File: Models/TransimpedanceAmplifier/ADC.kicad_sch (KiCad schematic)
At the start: 9 parts, among them U3 ADS8699IPW

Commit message: Save progress
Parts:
- U3: footprint PW16_TEX -> (none)
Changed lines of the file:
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@@
 			)
 		)
-		(property "Footprint" "PW16_TEX"
+		(property "Footprint" ""
 			(at 68.58 50.8 0)
 			(effects

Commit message: Save progress
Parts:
- U3: value ADS8699IPW -> ADS8699
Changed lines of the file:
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@@
 			)
 		)
-		(property "Value" "ADS8699IPW"
+		(property "Value" "ADS8699"
 			(at 104.14 43.18 0)
 			(effects

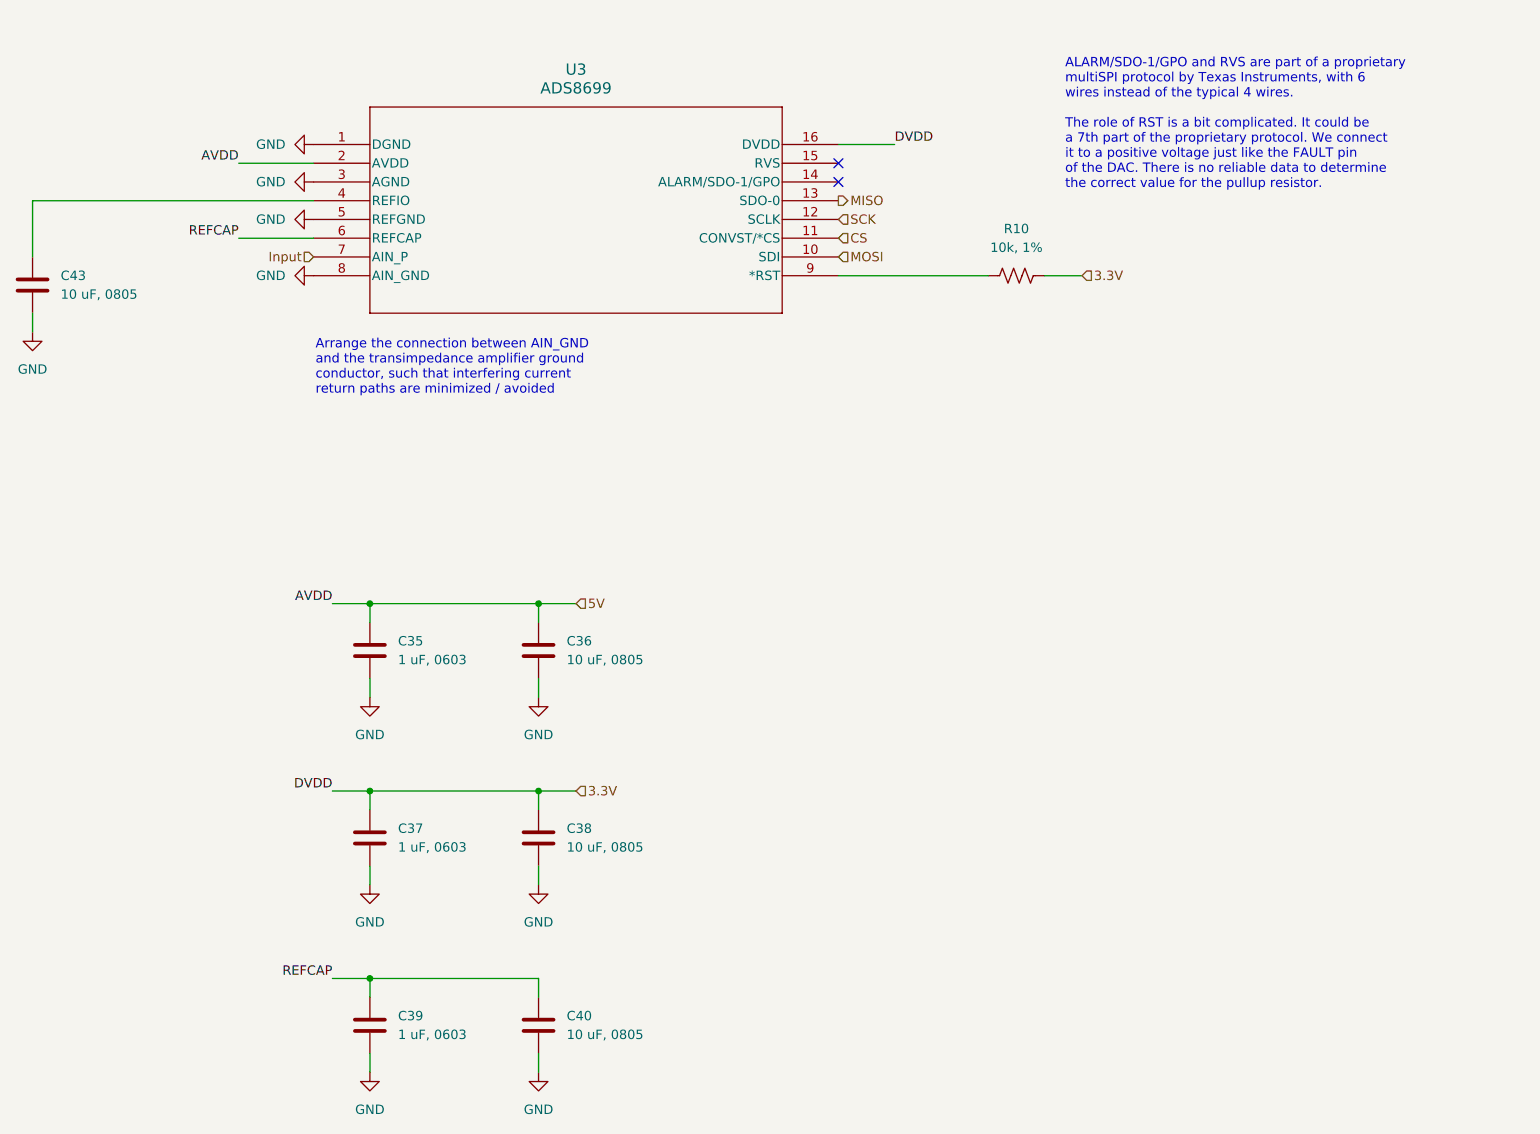
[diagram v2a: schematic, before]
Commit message: Overhauled all of the annotations
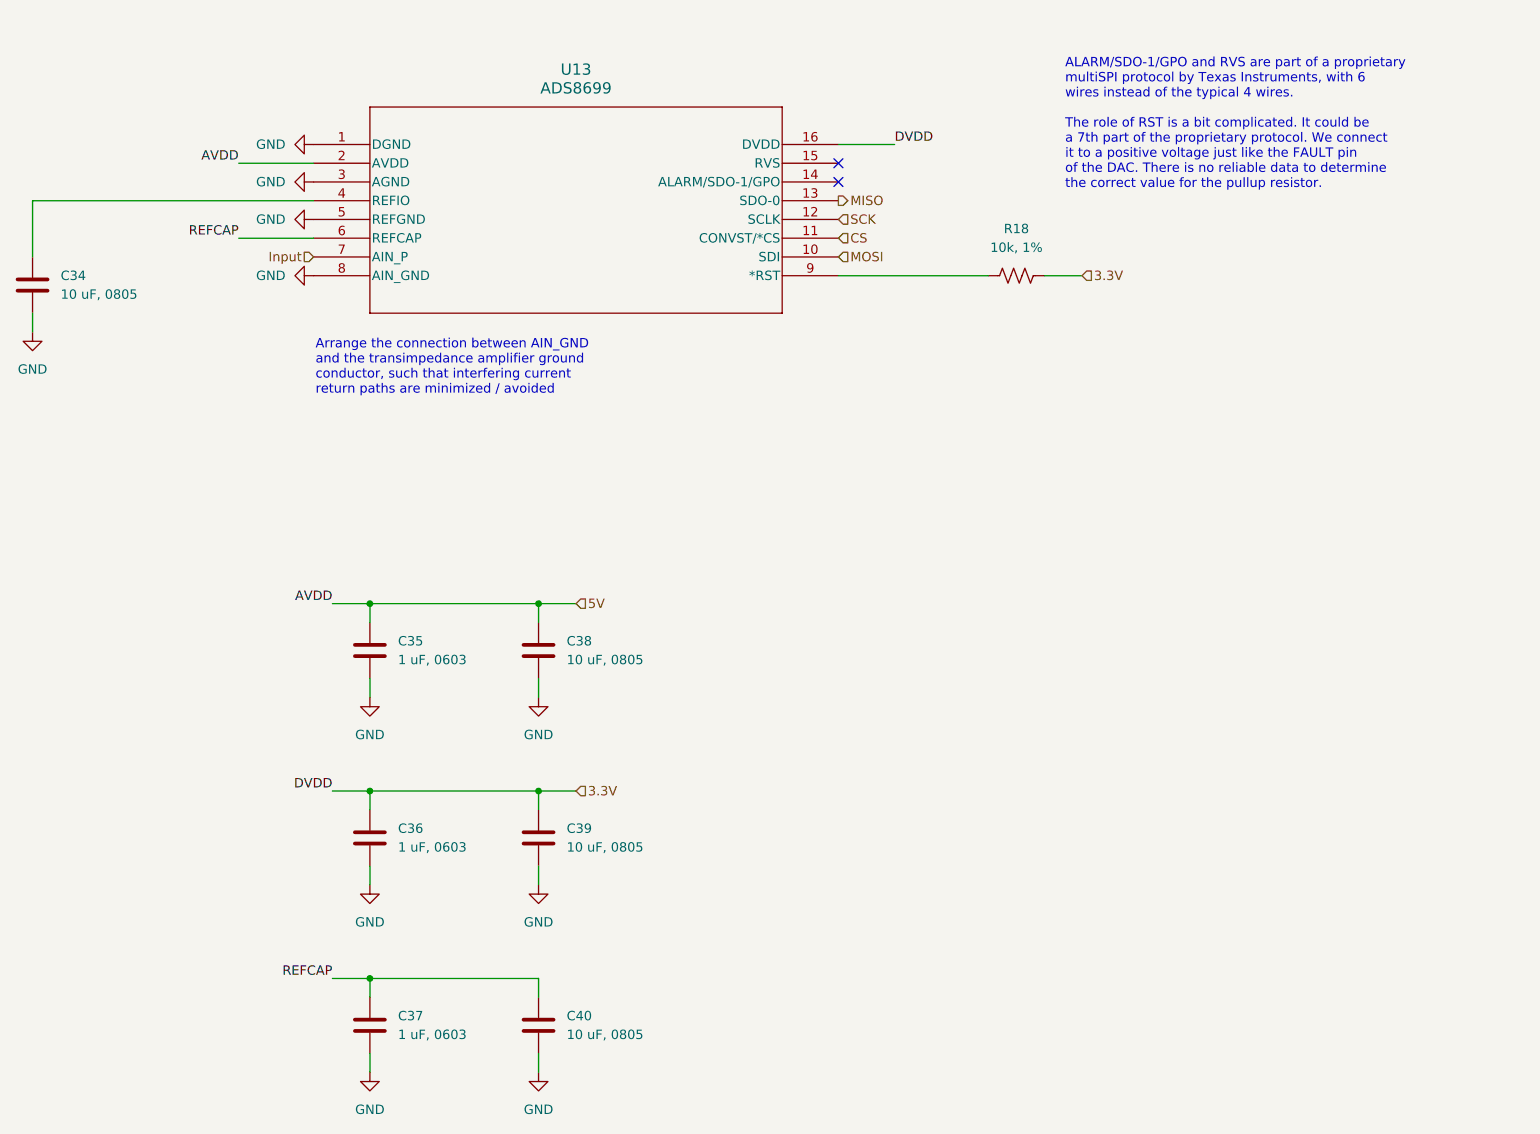
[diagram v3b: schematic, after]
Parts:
- renumbered C43 to C34, C37 to C36, C39 to C37, C36 to C38, C38 to C39, R10 to R18, U3 to U13
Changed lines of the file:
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@@
 		(dnp no)
 		(fields_autoplaced yes)
-		(property "Reference" "#PWR054"
+		(property "Reference" "#PWR056"
 			(at 99.06 182.88 0)
 			(effects
@@
 			(project "TransimpedanceAmplifier"
 				(path "/ec9f2ae3-e40d-40eb-9760-2b611ee8efd1/7e303428-a18c-4ad4-b002-5ab9c6631588/4e36751c-3edc-4fd3-bdbc-fcba4fce50b6"
-					(reference "#PWR054")
+					(reference "#PWR056")
 					(unit 1)
 				)
@@
 		(dnp no)
 		(fields_autoplaced yes)
-		(property "Reference" "#PWR051"
+		(property "Reference" "#PWR052"
 			(at 76.2 157.48 0)
 			(effects
@@
 			(project "TransimpedanceAmplifier"
 				(path "/ec9f2ae3-e40d-40eb-9760-2b611ee8efd1/7e303428-a18c-4ad4-b002-5ab9c6631588/4e36751c-3edc-4fd3-bdbc-fcba4fce50b6"
-					(reference "#PWR051")
+					(reference "#PWR052")
 					(unit 1)
 				)
@@
 		(dnp no)
 		(fields_autoplaced yes)
-		(property "Reference" "U3"
+		(property "Reference" "U13"
 			(at 104.14 40.64 0)
 			(effects
@@
 			(project ""
 				(path "/ec9f2ae3-e40d-40eb-9760-2b611ee8efd1/7e303428-a18c-4ad4-b002-5ab9c6631588/4e36751c-3edc-4fd3-bdbc-fcba4fce50b6"
-					(reference "U3")
+					(reference "U13")
 					(unit 1)
 				)
@@
 		(dnp no)
 		(fields_autoplaced yes)
-		(property "Reference" "#PWR057"
+		(property "Reference" "#PWR046"
 			(at 30.48 82.55 0)
 			(effects
@@
 			(project ""
 				(path "/ec9f2ae3-e40d-40eb-9760-2b611ee8efd1/7e303428-a18c-4ad4-b002-5ab9c6631588/4e36751c-3edc-4fd3-bdbc-fcba4fce50b6"
-					(reference "#PWR057")
+					(reference "#PWR046")
 					(unit 1)
 				)
@@
 		(dnp no)
 		(fields_autoplaced yes)
-		(property "Reference" "#PWR052"
+		(property "Reference" "#PWR055"
 			(at 99.06 157.48 0)
 			(effects
@@
 			(project "TransimpedanceAmplifier"
 				(path "/ec9f2ae3-e40d-40eb-9760-2b611ee8efd1/7e303428-a18c-4ad4-b002-5ab9c6631588/4e36751c-3edc-4fd3-bdbc-fcba4fce50b6"
-					(reference "#PWR052")
+					(reference "#PWR055")
 					(unit 1)
 				)
@@
 		(dnp no)
 		(fields_autoplaced yes)
-		(property "Reference" "C39"
+		(property "Reference" "C37"
 			(at 80.01 168.9099 0)
 			(effects
@@
 			(project "TransimpedanceAmplifier"
 				(path "/ec9f2ae3-e40d-40eb-9760-2b611ee8efd1/7e303428-a18c-4ad4-b002-5ab9c6631588/4e36751c-3edc-4fd3-bdbc-fcba4fce50b6"
-					(reference "C39")
+					(reference "C37")
 					(unit 1)
 				)
@@
 		(dnp no)
 		(fields_autoplaced yes)
-		(property "Reference" "C38"
+		(property "Reference" "C39"
 			(at 102.87 143.5099 0)
 			(effects
@@
 			(project "TransimpedanceAmplifier"
 				(path "/ec9f2ae3-e40d-40eb-9760-2b611ee8efd1/7e303428-a18c-4ad4-b002-5ab9c6631588/4e36751c-3edc-4fd3-bdbc-fcba4fce50b6"
-					(reference "C38")
+					(reference "C39")
 					(unit 1)
 				)
@@
 		(dnp no)
 		(fields_autoplaced yes)
-		(property "Reference" "C37"
+		(property "Reference" "C36"
 			(at 80.01 143.5099 0)
 			(effects
@@
 			(project "TransimpedanceAmplifier"
 				(path "/ec9f2ae3-e40d-40eb-9760-2b611ee8efd1/7e303428-a18c-4ad4-b002-5ab9c6631588/4e36751c-3edc-4fd3-bdbc-fcba4fce50b6"
-					(reference "C37")
+					(reference "C36")
 					(unit 1)
 				)
@@
 		(dnp no)
 		(fields_autoplaced yes)
-		(property "Reference" "#PWR017"
+		(property "Reference" "#PWR050"
 			(at 62.23 68.58 0)
 			(effects
@@
 			(project ""
 				(path "/ec9f2ae3-e40d-40eb-9760-2b611ee8efd1/7e303428-a18c-4ad4-b002-5ab9c6631588/4e36751c-3edc-4fd3-bdbc-fcba4fce50b6"
-					(reference "#PWR017")
+					(reference "#PWR050")
 					(unit 1)
 				)
@@
 		(dnp no)
 		(fields_autoplaced yes)
-		(property "Reference" "C36"
+		(property "Reference" "C38"
 			(at 102.87 118.1099 0)
 			(effects
@@
 			(project "TransimpedanceAmplifier"
 				(path "/ec9f2ae3-e40d-40eb-9760-2b611ee8efd1/7e303428-a18c-4ad4-b002-5ab9c6631588/4e36751c-3edc-4fd3-bdbc-fcba4fce50b6"
-					(reference "C36")
+					(reference "C38")
 					(unit 1)
 				)
@@
 		(dnp no)
 		(fields_autoplaced yes)
-		(property "Reference" "#PWR050"
+		(property "Reference" "#PWR054"
 			(at 99.06 132.08 0)
 			(effects
@@
 			(project "TransimpedanceAmplifier"
 				(path "/ec9f2ae3-e40d-40eb-9760-2b611ee8efd1/7e303428-a18c-4ad4-b002-5ab9c6631588/4e36751c-3edc-4fd3-bdbc-fcba4fce50b6"
-					(reference "#PWR050")
+					(reference "#PWR054")
 					(unit 1)
 				)
@@
 		(dnp no)
 		(fields_autoplaced yes)
-		(property "Reference" "#PWR049"
+		(property "Reference" "#PWR051"
 			(at 76.2 132.08 0)
 			(effects
@@
 			(project ""
 				(path "/ec9f2ae3-e40d-40eb-9760-2b611ee8efd1/7e303428-a18c-4ad4-b002-5ab9c6631588/4e36751c-3edc-4fd3-bdbc-fcba4fce50b6"
-					(reference "#PWR049")
+					(reference "#PWR051")
 					(unit 1)
 				)
@@
 		(dnp no)
 		(fields_autoplaced yes)
-		(property "Reference" "C43"
+		(property "Reference" "C34"
 			(at 34.29 68.5799 0)
 			(effects
@@
 			(project ""
 				(path "/ec9f2ae3-e40d-40eb-9760-2b611ee8efd1/7e303428-a18c-4ad4-b002-5ab9c6631588/4e36751c-3edc-4fd3-bdbc-fcba4fce50b6"
-					(reference "C43")
+					(reference "C34")
 					(unit 1)
 				)
@@
 		(dnp no)
 		(fields_autoplaced yes)
-		(property "Reference" "#PWR018"
+		(property "Reference" "#PWR049"
 			(at 62.23 60.96 0)
 			(effects
@@
 			(project "TransimpedanceAmplifier"
 				(path "/ec9f2ae3-e40d-40eb-9760-2b611ee8efd1/7e303428-a18c-4ad4-b002-5ab9c6631588/4e36751c-3edc-4fd3-bdbc-fcba4fce50b6"
-					(reference "#PWR018")
+					(reference "#PWR049")
 					(unit 1)
 				)
@@
 		(dnp no)
 		(fields_autoplaced yes)
-		(property "Reference" "R10"
+		(property "Reference" "R18"
 			(at 163.83 62.23 90)
 			(effects
@@
 			(project ""
 				(path "/ec9f2ae3-e40d-40eb-9760-2b611ee8efd1/7e303428-a18c-4ad4-b002-5ab9c6631588/4e36751c-3edc-4fd3-bdbc-fcba4fce50b6"
-					(reference "R10")
-					(unit 1)
-				)
+					(reference "R18")
+					(unit 1)
+				)

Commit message: Reorganized the DAC decoupling network for ease of modification
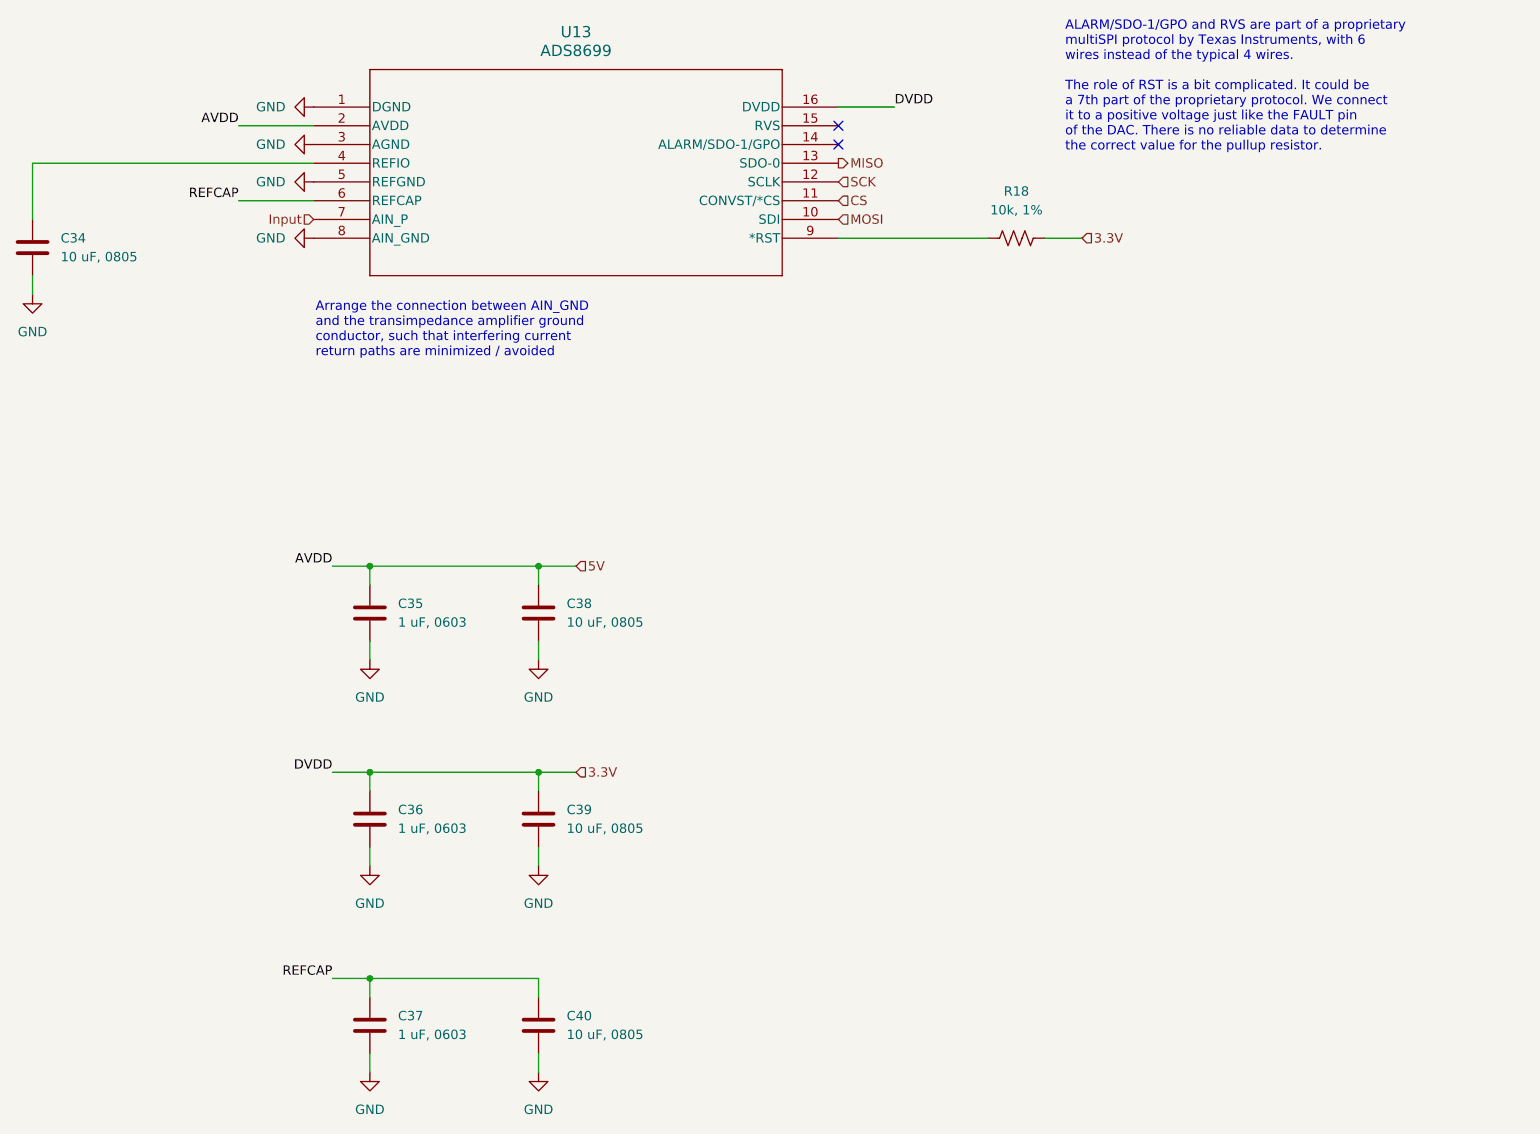
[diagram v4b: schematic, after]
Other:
- moved on the sheet: C34, C35, C36, C38, C39, R18, U13

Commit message: First successful ERC
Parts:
- added NT10, NT9: NetTie_2, symbol Device:NetTie_2
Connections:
- net 3.3V: now also NT10.2; no longer C36.1, C39.1, U13.16 (DVDD)
- net 5V: now also NT9.2; no longer C35.1, C38.1, U13.2 (AVDD)
- new net AVDD: C35.1, C38.1, NT9.1, U13.2 (AVDD)
- new net DVDD: C36.1, C39.1, NT10.1, U13.16 (DVDD)
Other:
- moved on the sheet: C35, C36, C37, C38, C39, C40

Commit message: Completely fixed the batteries
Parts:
- renumbered C38 to C37, C39 to C38, C37 to C39
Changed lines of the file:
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@@
 		(dnp no)
 		(fields_autoplaced yes)
-		(property "Reference" "#PWR056"
+		(property "Reference" "#PWR057"
 			(at 154.94 133.35 0)
 			(effects
@@
 			(project "TransimpedanceAmplifier"
 				(path "/ec9f2ae3-e40d-40eb-9760-2b611ee8efd1/7e303428-a18c-4ad4-b002-5ab9c6631588/4e36751c-3edc-4fd3-bdbc-fcba4fce50b6"
-					(reference "#PWR056")
+					(reference "#PWR057")
 					(unit 1)
 				)
@@
 		(on_board yes)
 		(dnp no)
-		(property "Reference" "#PWR052"
+		(property "Reference" "#PWR049"
 			(at 50.8 176.53 0)
 			(effects
@@
 			(project "TransimpedanceAmplifier"
 				(path "/ec9f2ae3-e40d-40eb-9760-2b611ee8efd1/7e303428-a18c-4ad4-b002-5ab9c6631588/4e36751c-3edc-4fd3-bdbc-fcba4fce50b6"
-					(reference "#PWR052")
+					(reference "#PWR049")
 					(unit 1)
 				)
@@
 		(dnp no)
 		(fields_autoplaced yes)
-		(property "Reference" "#PWR046"
+		(property "Reference" "#PWR047"
 			(at 30.48 77.47 0)
 			(effects
@@
 			(project ""
 				(path "/ec9f2ae3-e40d-40eb-9760-2b611ee8efd1/7e303428-a18c-4ad4-b002-5ab9c6631588/4e36751c-3edc-4fd3-bdbc-fcba4fce50b6"
-					(reference "#PWR046")
+					(reference "#PWR047")
 					(unit 1)
 				)
@@
 		(dnp no)
 		(fields_autoplaced yes)
-		(property "Reference" "C37"
+		(property "Reference" "C39"
 			(at 135.89 116.8399 0)
 			(effects
@@
 			(project "TransimpedanceAmplifier"
 				(path "/ec9f2ae3-e40d-40eb-9760-2b611ee8efd1/7e303428-a18c-4ad4-b002-5ab9c6631588/4e36751c-3edc-4fd3-bdbc-fcba4fce50b6"
-					(reference "C37")
+					(reference "C39")
 					(unit 1)
 				)
@@
 		(dnp no)
 		(fields_autoplaced yes)
-		(property "Reference" "C39"
+		(property "Reference" "C38"
 			(at 77.47 160.0199 0)
 			(effects
@@
 			(project "TransimpedanceAmplifier"
 				(path "/ec9f2ae3-e40d-40eb-9760-2b611ee8efd1/7e303428-a18c-4ad4-b002-5ab9c6631588/4e36751c-3edc-4fd3-bdbc-fcba4fce50b6"
-					(reference "C39")
+					(reference "C38")
 					(unit 1)
 				)
@@
 		(dnp no)
 		(fields_autoplaced yes)
-		(property "Reference" "#PWR053"
+		(property "Reference" "#PWR056"
 			(at 132.08 133.35 0)
 			(effects
@@
 			(project "TransimpedanceAmplifier"
 				(path "/ec9f2ae3-e40d-40eb-9760-2b611ee8efd1/7e303428-a18c-4ad4-b002-5ab9c6631588/4e36751c-3edc-4fd3-bdbc-fcba4fce50b6"
-					(reference "#PWR053")
+					(reference "#PWR056")
 					(unit 1)
 				)
@@
 		(dnp no)
 		(fields_autoplaced yes)
-		(property "Reference" "#PWR048"
+		(property "Reference" "#PWR051"
 			(at 62.23 50.8 0)
 			(effects
@@
 			(project "TransimpedanceAmplifier"
 				(path "/ec9f2ae3-e40d-40eb-9760-2b611ee8efd1/7e303428-a18c-4ad4-b002-5ab9c6631588/4e36751c-3edc-4fd3-bdbc-fcba4fce50b6"
-					(reference "#PWR048")
+					(reference "#PWR051")
 					(unit 1)
 				)
@@
 		(dnp no)
 		(fields_autoplaced yes)
-		(property "Reference" "#PWR050"
+		(property "Reference" "#PWR053"
 			(at 62.23 63.5 0)
 			(effects
@@
 			(project ""
 				(path "/ec9f2ae3-e40d-40eb-9760-2b611ee8efd1/7e303428-a18c-4ad4-b002-5ab9c6631588/4e36751c-3edc-4fd3-bdbc-fcba4fce50b6"
-					(reference "#PWR050")
+					(reference "#PWR053")
 					(unit 1)
 				)
@@
 		(dnp no)
 		(fields_autoplaced yes)
-		(property "Reference" "C38"
+		(property "Reference" "C37"
 			(at 77.47 116.8399 0)
 			(effects
@@
 			(project "TransimpedanceAmplifier"
 				(path "/ec9f2ae3-e40d-40eb-9760-2b611ee8efd1/7e303428-a18c-4ad4-b002-5ab9c6631588/4e36751c-3edc-4fd3-bdbc-fcba4fce50b6"
-					(reference "C38")
+					(reference "C37")
 					(unit 1)
 				)
@@
 		(on_board yes)
 		(dnp no)
-		(property "Reference" "#PWR051"
+		(property "Reference" "#PWR048"
 			(at 50.8 133.35 0)
 			(effects
@@
 			(project ""
 				(path "/ec9f2ae3-e40d-40eb-9760-2b611ee8efd1/7e303428-a18c-4ad4-b002-5ab9c6631588/4e36751c-3edc-4fd3-bdbc-fcba4fce50b6"
-					(reference "#PWR051")
+					(reference "#PWR048")
 					(unit 1)
 				)
@@
 		(dnp no)
 		(fields_autoplaced yes)
-		(property "Reference" "#PWR049"
+		(property "Reference" "#PWR052"
 			(at 62.23 55.88 0)
 			(effects
@@
 			(project "TransimpedanceAmplifier"
 				(path "/ec9f2ae3-e40d-40eb-9760-2b611ee8efd1/7e303428-a18c-4ad4-b002-5ab9c6631588/4e36751c-3edc-4fd3-bdbc-fcba4fce50b6"
-					(reference "#PWR049")
+					(reference "#PWR052")
 					(unit 1)
 				)
@@
 		(dnp no)
 		(fields_autoplaced yes)
-		(property "Reference" "#PWR047"
+		(property "Reference" "#PWR050"
 			(at 62.23 45.72 0)
 			(effects
@@
 			(project "TransimpedanceAmplifier"
 				(path "/ec9f2ae3-e40d-40eb-9760-2b611ee8efd1/7e303428-a18c-4ad4-b002-5ab9c6631588/4e36751c-3edc-4fd3-bdbc-fcba4fce50b6"
-					(reference "#PWR047")
-					(unit 1)
-				)
+					(reference "#PWR050")
+					(unit 1)
+				)

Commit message: Finalized the last detail of the schematic
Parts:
- renumbered R18 to R19
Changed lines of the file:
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@@
 		(dnp no)
 		(fields_autoplaced yes)
-		(property "Reference" "R18"
+		(property "Reference" "R19"
 			(at 163.83 57.15 90)
 			(effects
@@
 			(project ""
 				(path "/ec9f2ae3-e40d-40eb-9760-2b611ee8efd1/7e303428-a18c-4ad4-b002-5ab9c6631588/4e36751c-3edc-4fd3-bdbc-fcba4fce50b6"
-					(reference "R18")
+					(reference "R19")
 					(unit 1)
 				)
